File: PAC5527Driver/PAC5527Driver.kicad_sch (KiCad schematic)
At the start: 92 parts, among them J1 Conn_01x08, J2 Conn_01x04_MountingPin, J3 Conn_01x08_MountingPin, J4 Conn_01x03_MountingPin, J5 Conn_01x04_MountingPin, J6 Conn_01x04_MountingPin, J7 Conn_01x04_MountingPin, J8 Conn_01x04_MountingPin, J9 Conn_01x02, Q1 Si7336ADP, Q2 Si7336ADP, Q3 Si7336ADP, Q4 Si7336ADP, Q5 Si7336ADP, Q6 Si7336ADP, U1 USBLC6-2SC6, U2 PAC5527, U3 HT7533-1-SOT89, U4 SN65HVD233, U5 MA730

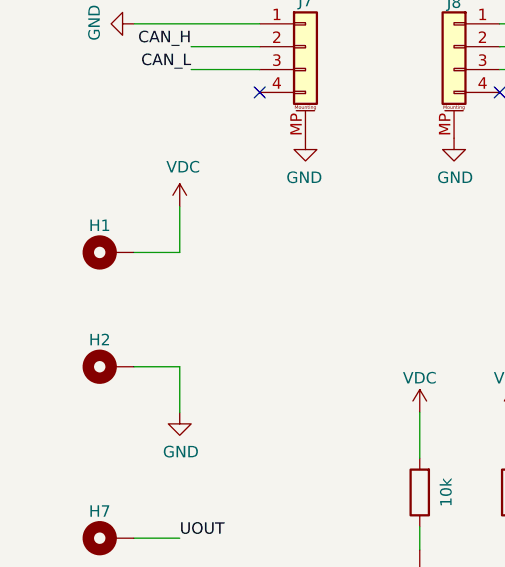
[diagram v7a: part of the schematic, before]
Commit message: GND stitch update
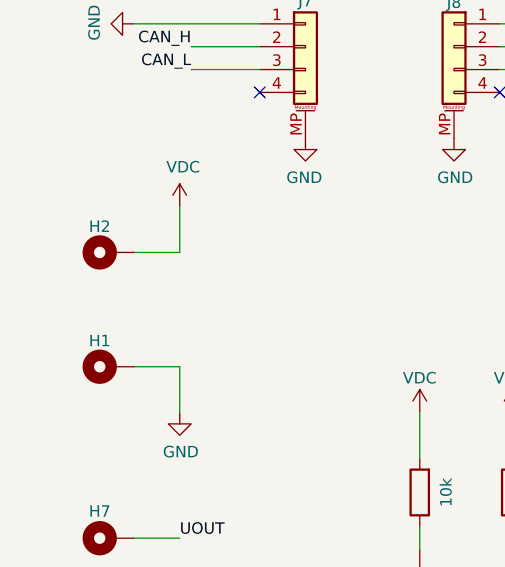
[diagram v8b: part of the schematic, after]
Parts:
- renumbered H2 to H1, H1 to H2
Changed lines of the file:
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@@
   (symbol (lib_id "Mechanical:MountingHole_Pad") (at 36.83 226.06 90) (unit 1)
     (in_bom yes) (on_board yes) (dnp no) (fields_autoplaced)
-    (property "Reference" "H1" (at 35.56 223.0905 90)
+    (property "Reference" "H2" (at 35.56 223.1931 90)
       (effects (font (size 1.27 1.27)))
     )
@@
       (project "PAC5527Driver"
         (path "/1ba3242e-22cf-4787-a878-8cbef96c3394"
-          (reference "H1") (unit 1)
+          (reference "H2") (unit 1)
         )
       )
@@
   (symbol (lib_id "Mechanical:MountingHole_Pad") (at 36.83 238.76 90) (unit 1)
     (in_bom yes) (on_board yes) (dnp no) (fields_autoplaced)
-    (property "Reference" "H2" (at 35.56 235.7905 90)
+    (property "Reference" "H1" (at 35.56 235.8931 90)
       (effects (font (size 1.27 1.27)))
     )
@@
       (project "PAC5527Driver"
         (path "/1ba3242e-22cf-4787-a878-8cbef96c3394"
-          (reference "H2") (unit 1)
-        )
-      )
+          (reference "H1") (unit 1)
+        )
+      )
